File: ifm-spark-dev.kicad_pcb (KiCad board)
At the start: 2 copper layers, 21 parts, among them J1 CONN_01X03_MALE, J2 CONN_01X06, J3 CONN_01X02, J4 CONN_01X07, J5 CONN_01X03_MALE, SW1 PTS525-SM15, U1 STM32F030x4, Y1 8MHz

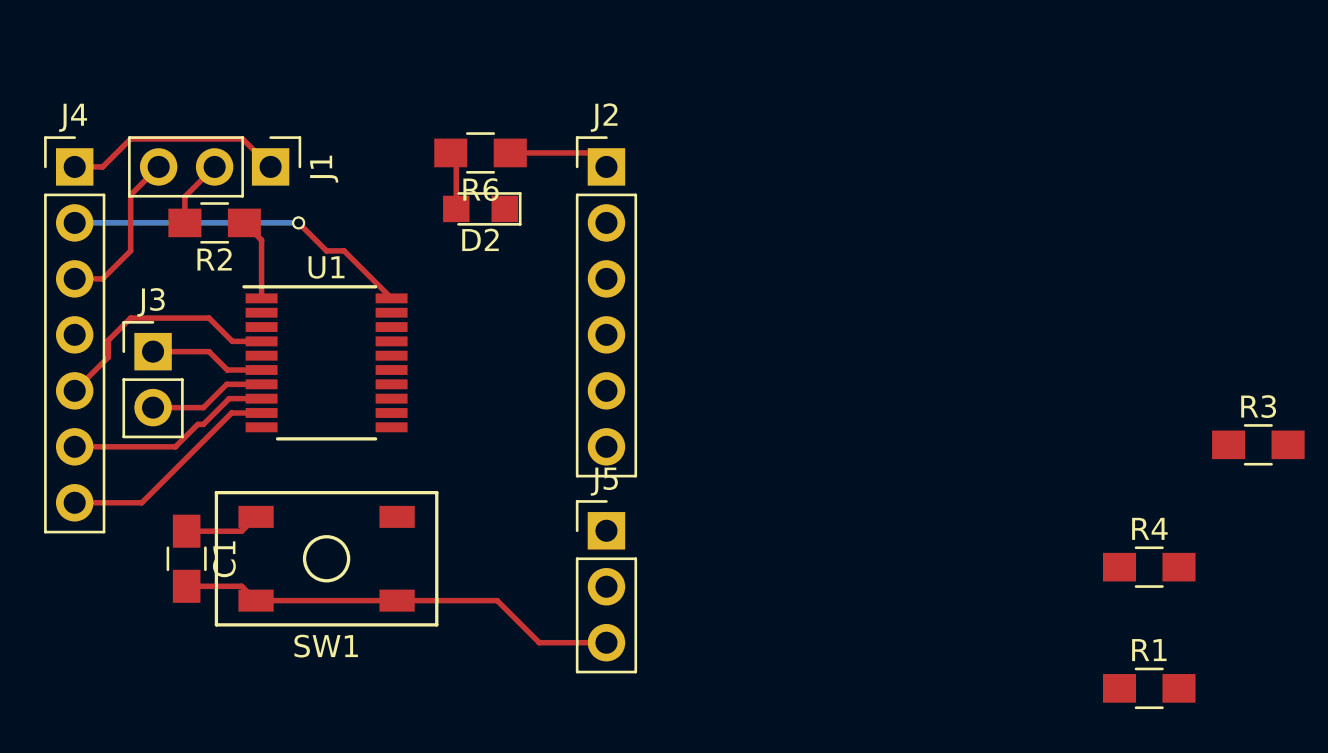
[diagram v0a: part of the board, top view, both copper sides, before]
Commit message: Rough hookup of extra GPIOs
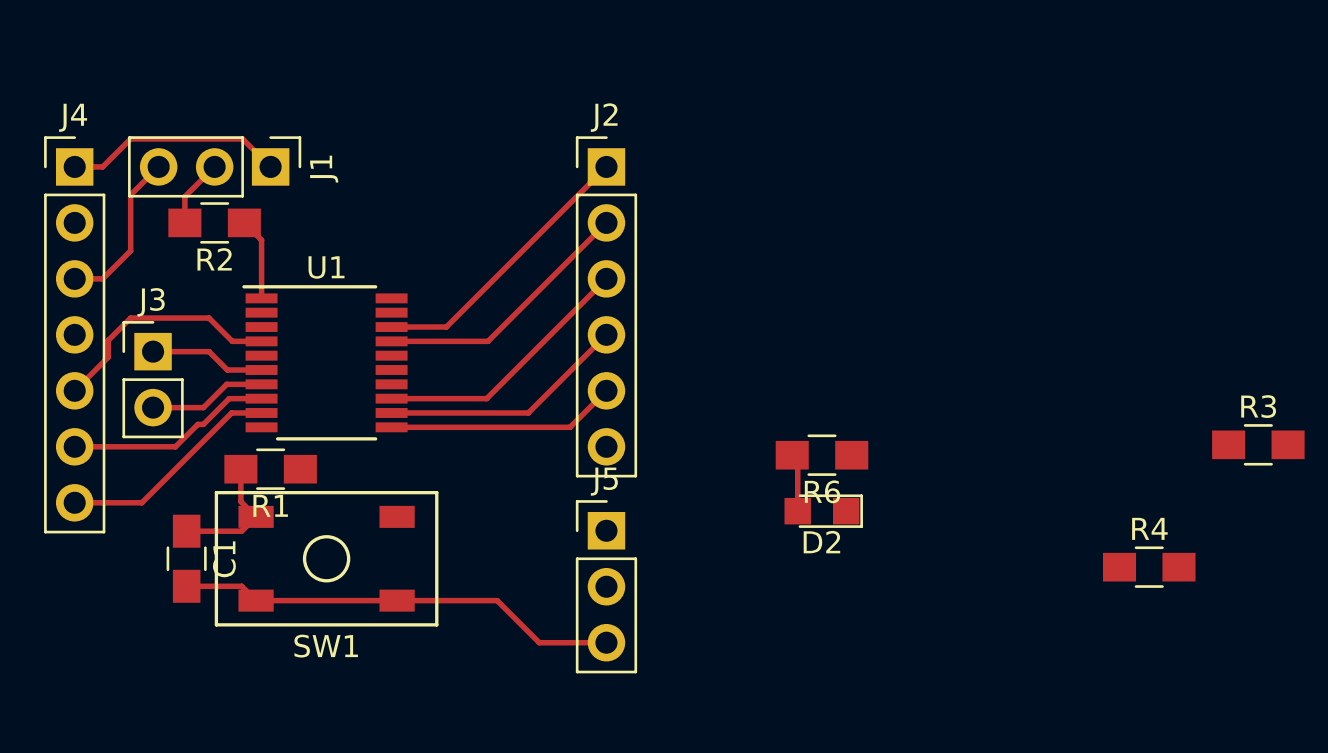
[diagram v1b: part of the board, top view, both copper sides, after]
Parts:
- moved R1 41.1 mm to (123.2, 102.6), turned to 180 degrees
- moved D2 20.7 mm to (148.2, 104.5)
- moved R6 20.7 mm to (148.2, 102.0)
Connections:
- J2 pad 1: /PA4 -> /PA10
- J2 pad 2: Net-(J2-Pad2) -> /PA9
- J2 pad 3: Net-(J2-Pad3) -> /PA7
- J2 pad 4: Net-(J2-Pad4) -> /PA6
- J2 pad 5: Net-(J2-Pad5) -> /PA5
- J2 pad 6: Net-(J2-Pad6) -> /PA4
- U1 pad 11: Net-(J2-Pad2) -> /PA5
- U1 pad 12: Net-(J2-Pad3) -> /PA6
- U1 pad 13: Net-(J2-Pad4) -> /PA7
- U1 pad 17: Net-(J2-Pad5) -> /PA9
- U1 pad 18: Net-(J2-Pad6) -> /PA10
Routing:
- net /SWCLK: track 15.8 -> 0.00 mm, vias 1 -> 0
- net /PA10: track 0.00 -> 12.8 mm
- net /PA7: track 0.00 -> 12.0 mm
- net /PA9: track 0.00 -> 12.0 mm
- net /PA6: track 0.00 -> 11.2 mm
- net /PA5: track 0.00 -> 10.4 mm
- net /PA4: track 4.63 -> 0.00 mm
- net Net-(C1-Pad1): track 3.42 -> 5.87 mm

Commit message: Update design rules to meet OSH Park minimums
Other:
- net class Default: via_dia 0.6 -> 0.7
- rule pad_to_mask_clearance: 0.2 -> 0
- rule via_min_drill: 0.3 -> 0.3302
- rule via_min_size: 0.4 -> 0.6858
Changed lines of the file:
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@@
   (general
     (links 48)
-    (no_connects 24)
+    (no_connects 42)
     (area 0 0 0 0)
     (thickness 1.6)
     (drawings 0)
-    (tracks 62)
+    (tracks 12)
     (zones 0)
     (modules 21)
@@
     (segment_width 0.2)
     (edge_width 0.15)
-    (via_size 0.6)
+    (via_size 0.7)
     (via_drill 0.4)
-    (via_min_size 0.4)
-    (via_min_drill 0.3)
-    (uvia_size 0.3)
-    (uvia_drill 0.1)
+    (via_min_size 0.6858)
+    (via_min_drill 0.3302)
+    (uvia_size 0.8)
+    (uvia_drill 0.51)
     (uvias_allowed no)
-    (uvia_min_size 0.2)
-    (uvia_min_drill 0.1)
+    (uvia_min_size 0)
+    (uvia_min_drill 0)
     (pcb_text_width 0.3)
     (pcb_text_size 1.5 1.5)
@@
     (pad_size 1.524 1.524)
     (pad_drill 0.762)
-    (pad_to_mask_clearance 0.2)
+    (pad_to_mask_clearance 0)
     (aux_axis_origin 0 0)
     (visible_elements FFFFFF7F)
@@
     (clearance 0.2)
     (trace_width 0.25)
-    (via_dia 0.6)
+    (via_dia 0.7)
     (via_drill 0.4)
-    (uvia_dia 0.3)
-    (uvia_drill 0.1)
+    (uvia_dia 0.8)
+    (uvia_drill 0.51)
     (add_net +3V3)
     (add_net /BOOT0)

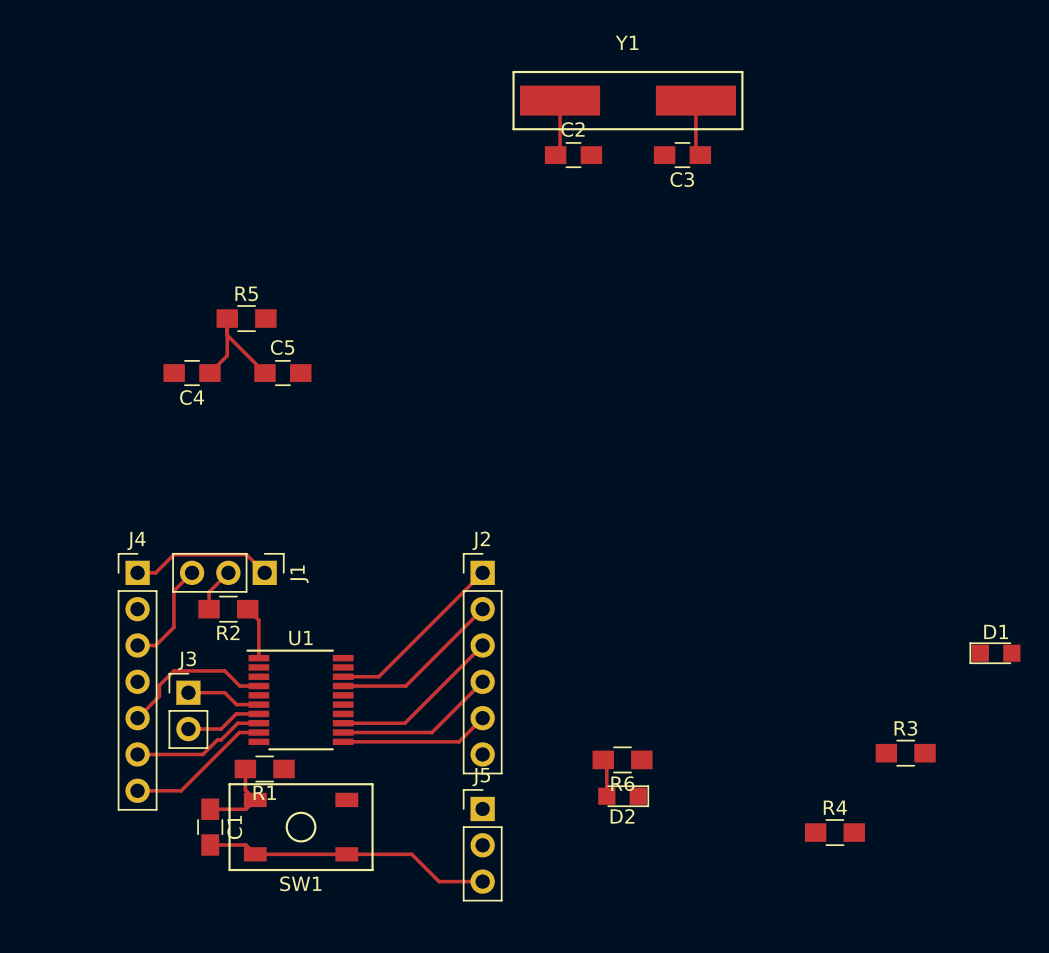
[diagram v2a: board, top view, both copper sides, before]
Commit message: First pass at connecting all nets on the board
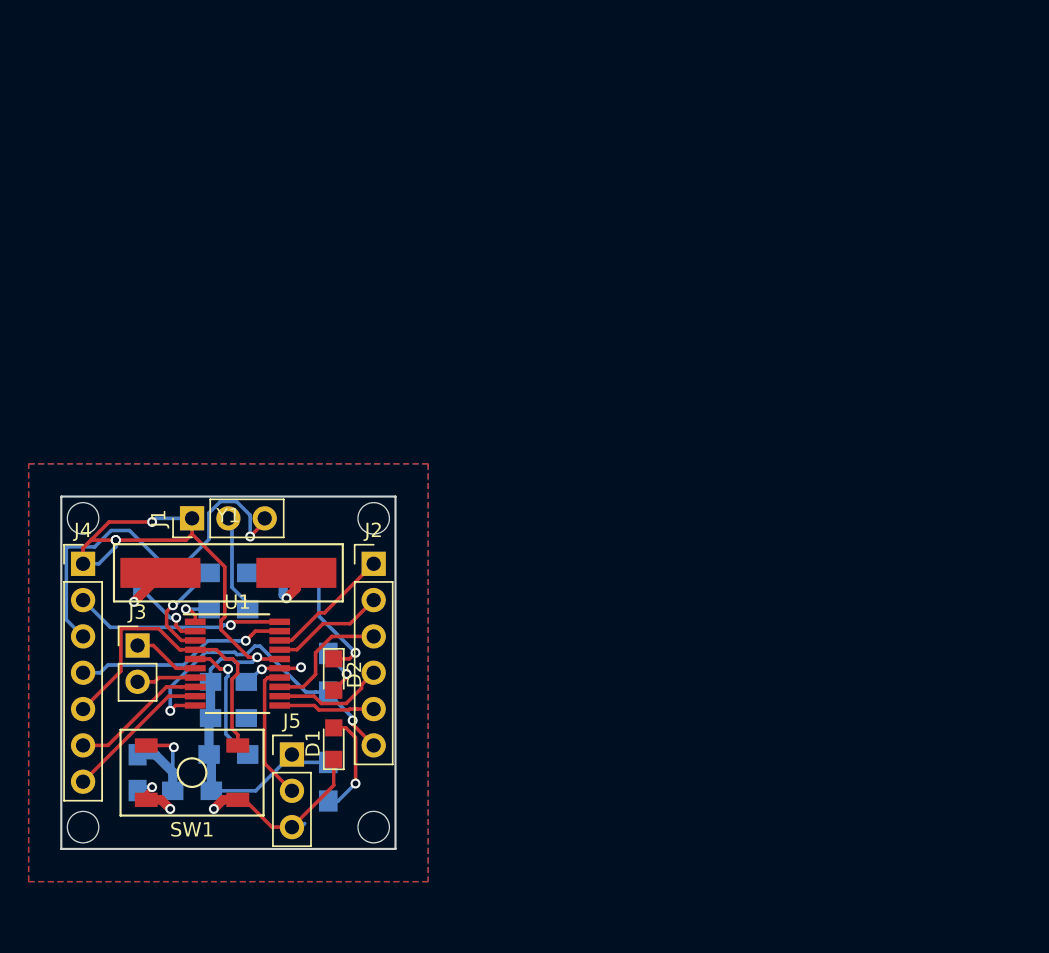
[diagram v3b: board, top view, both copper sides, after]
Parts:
- added REF**: MountingHole_2.2mm_M2, Mounting_Holes:MountingHole_2.2mm_M2, F.Cu at (130.8, 106.7)
- added REF**: MountingHole_2.2mm_M2, Mounting_Holes:MountingHole_2.2mm_M2, F.Cu at (110.5, 106.7)
- added REF**: MountingHole_2.2mm_M2, Mounting_Holes:MountingHole_2.2mm_M2, F.Cu at (110.5, 85.1)
- added REF**: MountingHole_2.2mm_M2, Mounting_Holes:MountingHole_2.2mm_M2, F.Cu at (130.8, 85.1)
- C1, C2, C3, C4, C5, R1, R2, R3, R4, R5, R6: moved to B.Cu
- moved R3 49.0 mm to (120.7, 88.9)
- moved D1 46.7 mm to (128.0, 100.8), turned to 90 degrees
- moved Y1 43.3 mm to (120.7, 88.9)
- moved C2 41.3 mm to (115.6, 88.9)
- moved C3 39.6 mm to (125.7, 88.9), turned to 0 degrees
- moved R4 35.6 mm to (127.6, 103.5), turned to 90 degrees
- moved R5 30.5 mm to (120.7, 101.6)
- moved C4 24.3 mm to (120.7, 99.1), turned to 0 degrees
- moved C5 21.9 mm to (120.7, 96.5)
- moved D2 21.9 mm to (128.0, 96.0), turned to 270 degrees
- moved R6 21.5 mm to (127.6, 95.9), turned to 90 degrees
- moved J5 13.9 mm to (125.1, 101.6)
- moved SW1 8.52 mm to (118.1, 102.9)
- moved J2 7.65 mm to (130.8, 88.3)
- moved C1 6.35 mm to (114.3, 102.9)
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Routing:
- net +3V3: track 19.2 -> 56.5 mm, vias 0 -> 4
- net GND: track 27.5 -> 58.2 mm, vias 0 -> 7
- net /PA4: track 0.00 -> 22.3 mm, vias 0 -> 2
- net /SWDIO: track 0.00 -> 15.0 mm, vias 0 -> 1
- net /SWCLK: track 0.00 -> 14.7 mm, vias 0 -> 1
- net /NRST: track 10.7 -> 21.9 mm
- net /IR_SIGNAL: track 0.00 -> 9.63 mm
- net Net-(R5-Pad2): track 0.00 -> 9.31 mm, vias 0 -> 1
- net Net-(C2-Pad1): track 3.94 -> 11.5 mm, vias 0 -> 2
- net Net-(R3-Pad1): track 0.00 -> 7.51 mm, vias 0 -> 1
- net Net-(D1-Pad2): track 0.00 -> 7.43 mm, vias 0 -> 1
- net /PA9: track 12.0 -> 8.01 mm
- net /PA10: track 12.8 -> 8.80 mm
- net Net-(J1-Pad2): track 3.10 -> 6.91 mm
- net /PA5: track 10.4 -> 6.73 mm
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- added copper zone on F.Cu, net +3V3
- added copper zone on B.Cu, net GND
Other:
- board outline added: 23.4 x 24.6 mm
